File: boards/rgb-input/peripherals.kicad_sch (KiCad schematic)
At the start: 15 parts, among them J2 I2C

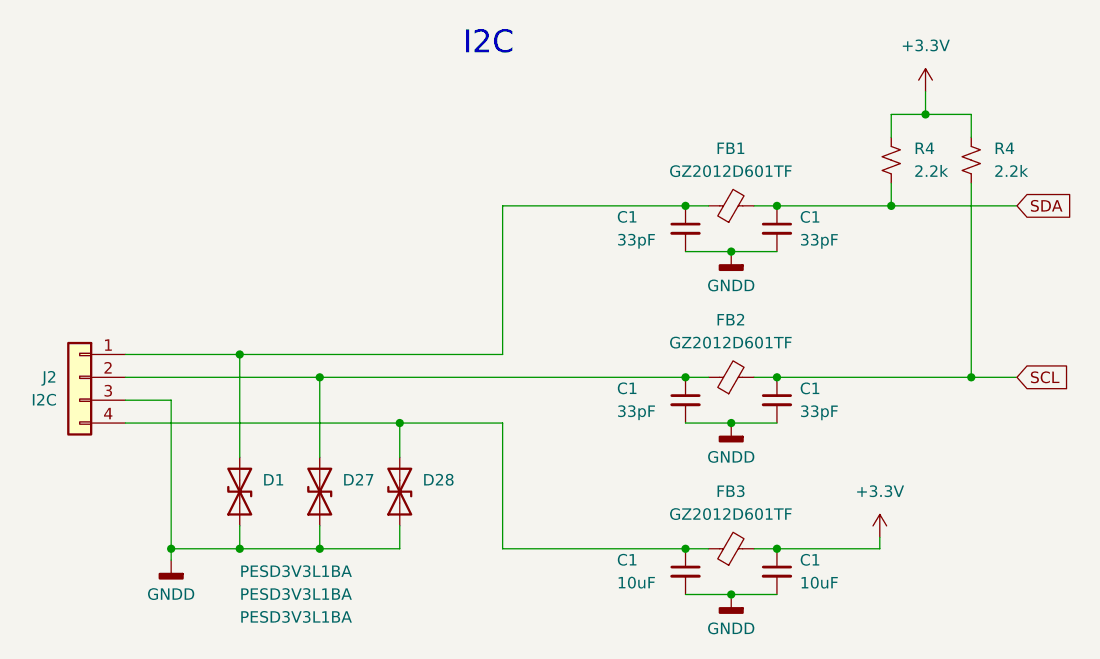
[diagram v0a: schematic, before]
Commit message: more layout checks on the input board
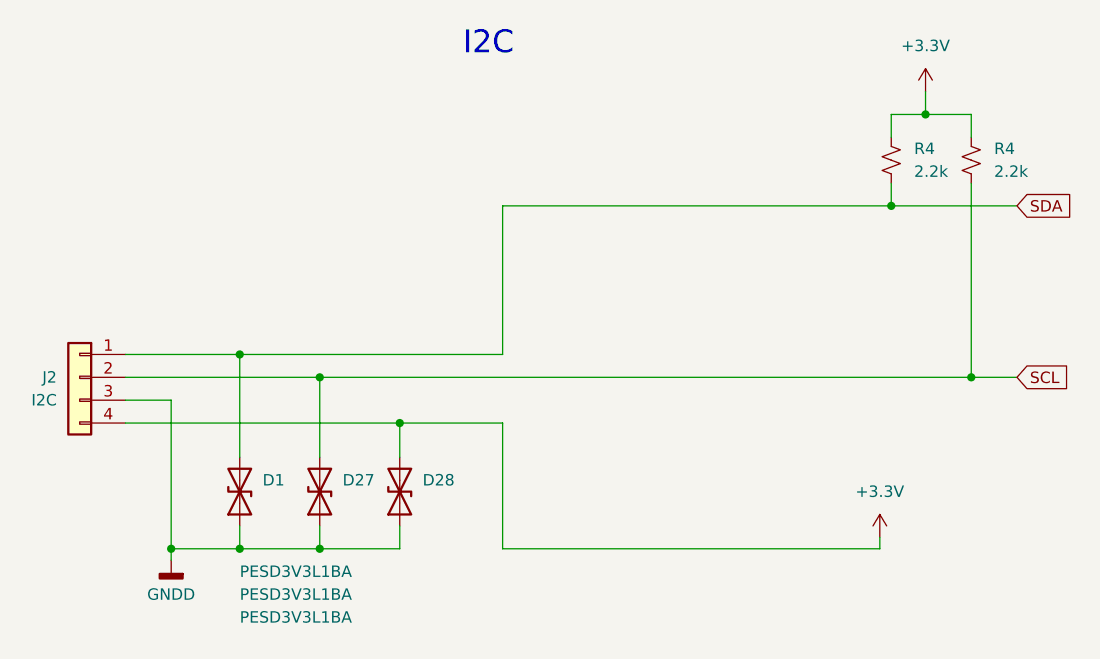
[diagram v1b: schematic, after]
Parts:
- removed C1 (x4): 33pF, Capacitor_SMD:C_0805_2012Metric_Pad1.18x1.45mm_HandSolder, symbol Device:C_Small
- removed C1 (x2): 10uF, Capacitor_SMD:C_0805_2012Metric_Pad1.18x1.45mm_HandSolder, symbol Device:C_Small
- removed FB1, FB2, FB3: GZ2012D601TF, Inductor_SMD:L_0805_2012Metric, symbol Device:FerriteBead_Small
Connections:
- net +3.3V: now also D28.2 (A2), J2.4 (Pin_4)
- net SCL: now also D27.2 (A2), J2.2 (Pin_2)
- net SDA: now also D1.2 (A2), J2.1 (Pin_1)

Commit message: routed the rgb setup
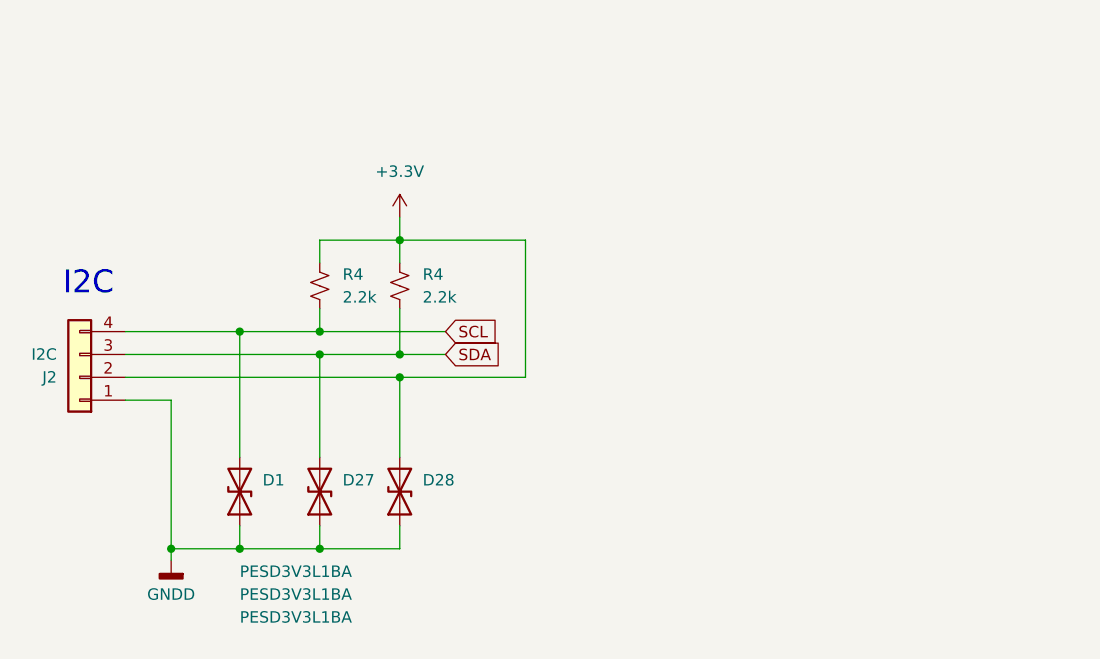
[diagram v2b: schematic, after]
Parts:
- J2: footprint Connector_PinHeader_2.54mm:PinHeader_1x04_P2.54mm_Vertical -> Connector_JST:JST_SH_SM04B-SRSS-TB_1x04-1MP_P1.00mm_Horizontal; Vendor (none) -> SM04B-SRSS-TB
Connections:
- net +3.3V: now also J2.2 (Pin_2); no longer J2.4 (Pin_4)
- net GNDD: now also J2.1 (Pin_1); no longer J2.3 (Pin_3)
- net SCL: now also D1.2 (A2), J2.4 (Pin_4), R4.1; no longer D27.2 (A2), J2.2 (Pin_2), R4.1
- net SDA: now also D27.2 (A2), J2.3 (Pin_3), R4.1; no longer D1.2 (A2), J2.1 (Pin_1), R4.1
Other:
- moved on the sheet: J2, R4

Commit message: various cleanups and tidying
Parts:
- J2: symbol Connector_Generic:Conn_01x04 -> Connector_Generic_MountingPin:Conn_01x04_MountingPin
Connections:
- no-connect marks 0 -> 1
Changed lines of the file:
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@@
   (junction (at 175.26 100.33) (diameter 0) (color 0 0 0 0)
   )
+  (no_connect (at 165.1 71.12))
   (wire (pts (xy 191.77 100.33) (xy 191.77 97.79))
     (stroke (width 0) (type default))
@@
     (stroke (width 0) (type default))
   )
-  (text "I2C" (at 168.91 72.39 0)
+  (text "I2C" (at 175.895 72.39 0)
     (effects (font (size 2.54 2.54)) (justify right bottom))
   )
@@
     )
   )
-  (symbol (lib_id "Connector_Generic:Conn_01x04") (at 165.1 81.28 180) (unit 1)
+  (symbol (lib_id "Connector_Generic_MountingPin:Conn_01x04_MountingPin") (at 165.1 81.28 180) (unit 1)
     (in_bom yes) (on_board yes) (dnp no)
     (property "Reference" "J2" (at 162.56 81.28 0)
@@
     (pin "3")
     (pin "4")
+    (pin "MP")
     (instances
       (project "rgb-input"

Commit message: more BOM updates.
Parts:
- D1, D27, D28: footprint Diode_SMD:D_SOD-323_HandSoldering -> Diode_SMD:D_SOD-323; LCSC (none) -> C316020
- J2: LCSC (none) -> C160404; Vendor SM04B-SRSS-TB -> (none)
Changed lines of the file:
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@@
       (effects (font (size 1.27 1.27)) (justify right))
     )
-    (property "Footprint" "Diode_SMD:D_SOD-323_HandSoldering" (at 200.66 93.98 0)
+    (property "Footprint" "Diode_SMD:D_SOD-323" (at 200.66 93.98 0)
       (effects (font (size 1.27 1.27)) hide)
     )
     (property "Datasheet" "~" (at 200.66 93.98 0)
+      (effects (font (size 1.27 1.27)) hide)
+    )
+    (property "LCSC" "C316020" (at 200.66 93.98 90)
       (effects (font (size 1.27 1.27)) hide)
     )
@@
       (effects (font (size 1.27 1.27)) (justify right))
     )
-    (property "Footprint" "Diode_SMD:D_SOD-323_HandSoldering" (at 182.88 93.98 0)
+    (property "Footprint" "Diode_SMD:D_SOD-323" (at 182.88 93.98 0)
       (effects (font (size 1.27 1.27)) hide)
     )
     (property "Datasheet" "~" (at 182.88 93.98 0)
+      (effects (font (size 1.27 1.27)) hide)
+    )
+    (property "LCSC" "C316020" (at 182.88 93.98 90)
       (effects (font (size 1.27 1.27)) hide)
     )
@@
       (effects (font (size 1.27 1.27)) hide)
     )
-    (property "Vendor" "SM04B-SRSS-TB" (at 165.1 81.28 0)
+    (property "LCSC" "C160404" (at 165.1 81.28 0)
       (effects (font (size 1.27 1.27)) hide)
     )
@@
       (effects (font (size 1.27 1.27)) (justify right))
     )
-    (property "Footprint" "Diode_SMD:D_SOD-323_HandSoldering" (at 191.77 93.98 0)
+    (property "Footprint" "Diode_SMD:D_SOD-323" (at 191.77 93.98 0)
       (effects (font (size 1.27 1.27)) hide)
     )
@@
       (effects (font (size 1.27 1.27)) hide)
     )
+    (property "LCSC" "C316020" (at 191.77 93.98 90)
+      (effects (font (size 1.27 1.27)) hide)
+    )

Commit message: new rgb input board is starting to look very nice.
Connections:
- net GNDD: now also J2.MP (MountPin)
- no-connect marks 1 -> 0
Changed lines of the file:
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@@
   (junction (at 175.26 100.33) (diameter 0) (color 0 0 0 0)
   )
-  (no_connect (at 165.1 71.12))
   (wire (pts (xy 191.77 100.33) (xy 191.77 97.79))
     (stroke (width 0) (type default))
@@
         )
       )
+    )
+  )
+  (symbol (lib_id "power:GNDD") (at 165.1 71.12 0) (mirror x) (unit 1)
+    (in_bom yes) (on_board yes) (dnp no) (fields_autoplaced)
+    (property "Reference" "#PWR054" (at 165.1 64.77 0)
+      (effects (font (size 1.27 1.27)) hide)
+    )
+    (property "Value" "GNDD" (at 165.1 67.31 0)
+      (effects (font (size 1.27 1.27)))
+    )
+    (property "Footprint" "" (at 165.1 71.12 0)
+      (effects (font (size 1.27 1.27)) hide)
+    )
+    (property "Datasheet" "" (at 165.1 71.12 0)
+      (effects (font (size 1.27 1.27)) hide)
+    )
+    (pin "1")
+    (instances
+      (project "rgb-input"
+        (path "/c83c6236-96e9-46ad-9d7a-9e2efa4a7966"
+          (reference "#PWR054") (unit 1)
+        )
+        (path "/c83c6236-96e9-46ad-9d7a-9e2efa4a7966/0036d08f-39b5-4a29-8e4d-ea832b2cc879"
+          (reference "#PWR035") (unit 1)
+        )
+      )

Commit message: reannotated and did some more cleanup.  almost ready
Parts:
- renumbered D27 to D2, D28 to D3
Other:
- company: (none) -> github.com/hoeken/yarrboard
- title: (none) -> RGB Input Board
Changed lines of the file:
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@@
 (kicad_sch (version 20230121) (generator eeschema)
   (paper "A4")
+  (title_block
+    (title "RGB Input Board")
+    (rev "B")
+    (company "github.com/hoeken/yarrboard")
+    (comment 1 "Open Source Hardware")
+  )
   (junction (at 182.88 100.33) (diameter 0) (color 0 0 0 0)
   )
@@
   (symbol (lib_id "Device:D_TVS") (at 200.66 93.98 90) (unit 1)
     (in_bom yes) (on_board yes) (dnp no)
-    (property "Reference" "D28" (at 203.2 92.71 90)
+    (property "Reference" "D3" (at 203.2 92.71 90)
       (effects (font (size 1.27 1.27)) (justify right))
     )
@@
       (project "rgb-input"
         (path "/c83c6236-96e9-46ad-9d7a-9e2efa4a7966/0036d08f-39b5-4a29-8e4d-ea832b2cc879"
-          (reference "D28") (unit 1)
+          (reference "D3") (unit 1)
         )
       )
@@
         )
         (path "/c83c6236-96e9-46ad-9d7a-9e2efa4a7966/0036d08f-39b5-4a29-8e4d-ea832b2cc879"
-          (reference "#PWR035") (unit 1)
+          (reference "#PWR08") (unit 1)
         )
       )
@@
         )
         (path "/c83c6236-96e9-46ad-9d7a-9e2efa4a7966/0036d08f-39b5-4a29-8e4d-ea832b2cc879"
-          (reference "J13") (unit 1)
+          (reference "J2") (unit 1)
         )
       )
@@
         )
         (path "/c83c6236-96e9-46ad-9d7a-9e2efa4a7966/0036d08f-39b5-4a29-8e4d-ea832b2cc879"
-          (reference "#PWR076") (unit 1)
+          (reference "#PWR07") (unit 1)
         )
       )
@@
         )
         (path "/c83c6236-96e9-46ad-9d7a-9e2efa4a7966/0036d08f-39b5-4a29-8e4d-ea832b2cc879"
-          (reference "R42") (unit 1)
+          (reference "R3") (unit 1)
         )
       )
@@
         )
         (path "/c83c6236-96e9-46ad-9d7a-9e2efa4a7966/0036d08f-39b5-4a29-8e4d-ea832b2cc879"
-          (reference "#PWR061") (unit 1)
+          (reference "#PWR09") (unit 1)
         )
       )
@@
         )
         (path "/c83c6236-96e9-46ad-9d7a-9e2efa4a7966/0036d08f-39b5-4a29-8e4d-ea832b2cc879"
-          (reference "R40") (unit 1)
+          (reference "R2") (unit 1)
         )
       )
@@
   (symbol (lib_id "Device:D_TVS") (at 191.77 93.98 90) (unit 1)
     (in_bom yes) (on_board yes) (dnp no)
-    (property "Reference" "D27" (at 194.31 92.71 90)
+    (property "Reference" "D2" (at 194.31 92.71 90)
       (effects (font (size 1.27 1.27)) (justify right))
     )
@@
       (project "rgb-input"
         (path "/c83c6236-96e9-46ad-9d7a-9e2efa4a7966/0036d08f-39b5-4a29-8e4d-ea832b2cc879"
-          (reference "D27") (unit 1)
-        )
-      )
+          (reference "D2") (unit 1)
+        )
+      )
